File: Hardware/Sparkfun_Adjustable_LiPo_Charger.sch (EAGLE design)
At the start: 25 parts, among them SW1 DIP-06, U1 MCP73831

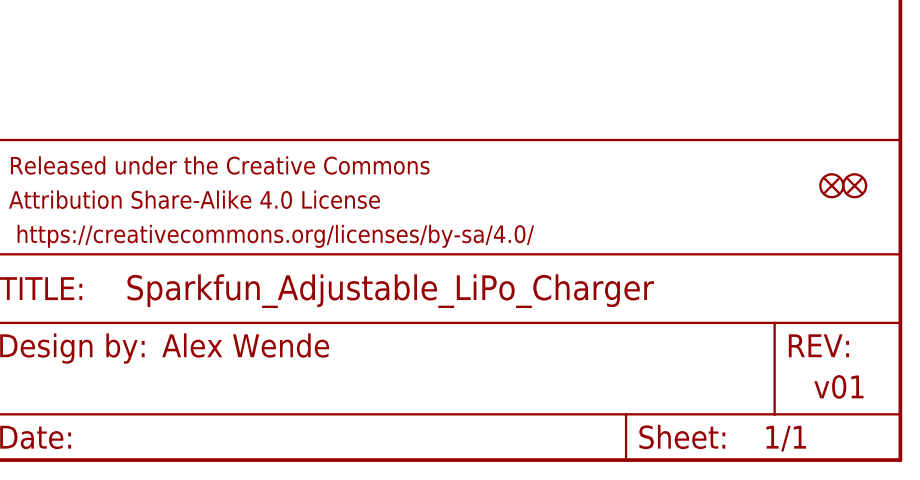
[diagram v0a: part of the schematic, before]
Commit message: Design Review Changes
Replaced PTH coin cell holder with SMD
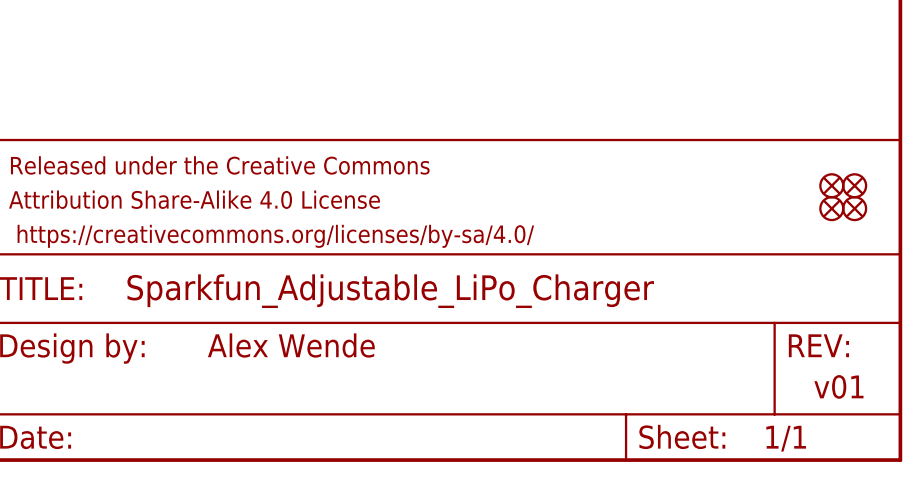
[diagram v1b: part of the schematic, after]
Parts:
- added FD3, FD4: FIDUCIALUFIDUCIAL, SparkFun-Aesthetics:FIDUCIALUFIDUCIAL
- BT1: device SparkFun-Batteries:BATTERY-24.5MM_PTH -> SparkFun-Batteries:BATTERY-24.5MM_SMD
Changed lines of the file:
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@@
 <grid distance="0.1" unitdist="inch" unit="inch" style="lines" multiple="1" display="no" altdistance="0.01" altunitdist="inch" altunit="inch"/>
 <layers>
-<layer number="1" name="Top" color="4" fill="1" visible="yes" active="no"/>
-<layer number="2" name="Route2" color="1" fill="3" visible="yes" active="no"/>
-<layer number="3" name="Route3" color="4" fill="3" visible="yes" active="no"/>
-<layer number="4" name="Route4" color="1" fill="4" visible="yes" active="no"/>
-<layer number="5" name="Route5" color="4" fill="4" visible="yes" active="no"/>
-<layer number="6" name="Route6" color="1" fill="8" visible="yes" active="no"/>
-<layer number="7" name="Route7" color="4" fill="8" visible="yes" active="no"/>
-<layer number="8" name="Route8" color="1" fill="2" visible="yes" active="no"/>
-<layer number="9" name="Route9" color="4" fill="2" visible="yes" active="no"/>
-<layer number="10" name="Route10" color="1" fill="7" visible="yes" active="no"/>
-<layer number="11" name="Route11" color="4" fill="7" visible="yes" active="no"/>
-<layer number="12" name="Route12" color="1" fill="5" visible="yes" active="no"/>
-<layer number="13" name="Route13" color="4" fill="5" visible="yes" active="no"/>
-<layer number="14" name="Route14" color="1" fill="6" visible="yes" active="no"/>
-<layer number="15" name="Route15" color="4" fill="6" visible="yes" active="no"/>
-<layer number="16" name="Bottom" color="1" fill="1" visible="yes" active="no"/>
-<layer number="17" name="Pads" color="2" fill="1" visible="yes" active="no"/>
-<layer number="18" name="Vias" color="2" fill="1" visible="yes" active="no"/>
-<layer number="19" name="Unrouted" color="6" fill="1" visible="yes" active="no"/>
-<layer number="20" name="Dimension" color="15" fill="1" visible="yes" active="no"/>
-<layer number="21" name="tPlace" color="16" fill="1" visible="yes" active="no"/>
-<layer number="22" name="bPlace" color="14" fill="1" visible="yes" active="no"/>
-<layer number="23" name="tOrigins" color="15" fill="1" visible="yes" active="no"/>
-<layer number="24" name="bOrigins" color="15" fill="1" visible="yes" active="no"/>
-<layer number="25" name="tNames" color="7" fill="1" visible="yes" active="no"/>
-<layer number="26" name="bNames" color="7" fill="1" visible="yes" active="no"/>
-<layer number="27" name="tValues" color="7" fill="1" visible="yes" active="no"/>
-<layer number="28" name="bValues" color="7" fill="1" visible="yes" active="no"/>
+<layer number="1" name="Top" color="4" fill="1" visible="no" active="no"/>
+<layer number="2" name="Route2" color="1" fill="3" visible="no" active="no"/>
+<layer number="3" name="Route3" color="4" fill="3" visible="no" active="no"/>
+<layer number="4" name="Route4" color="1" fill="4" visible="no" active="no"/>
+<layer number="5" name="Route5" color="4" fill="4" visible="no" active="no"/>
+<layer number="6" name="Route6" color="1" fill="8" visible="no" active="no"/>
+<layer number="7" name="Route7" color="4" fill="8" visible="no" active="no"/>
+<layer number="8" name="Route8" color="1" fill="2" visible="no" active="no"/>
+<layer number="9" name="Route9" color="4" fill="2" visible="no" active="no"/>
+<layer number="10" name="Route10" color="1" fill="7" visible="no" active="no"/>
+<layer number="11" name="Route11" color="4" fill="7" visible="no" active="no"/>
+<layer number="12" name="Route12" color="1" fill="5" visible="no" active="no"/>
+<layer number="13" name="Route13" color="4" fill="5" visible="no" active="no"/>
+<layer number="14" name="Route14" color="1" fill="6" visible="no" active="no"/>
+<layer number="15" name="Route15" color="4" fill="6" visible="no" active="no"/>
+<layer number="16" name="Bottom" color="1" fill="1" visible="no" active="no"/>
+<layer number="17" name="Pads" color="2" fill="1" visible="no" active="no"/>
+<layer number="18" name="Vias" color="2" fill="1" visible="no" active="no"/>
+<layer number="19" name="Unrouted" color="6" fill="1" visible="no" active="no"/>
+<layer number="20" name="Dimension" color="15" fill="1" visible="no" active="no"/>
+<layer number="21" name="tPlace" color="16" fill="1" visible="no" active="no"/>
+<layer number="22" name="bPlace" color="14" fill="1" visible="no" active="no"/>
+<layer number="23" name="tOrigins" color="15" fill="1" visible="no" active="no"/>
+<layer number="24" name="bOrigins" color="15" fill="1" visible="no" active="no"/>
+<layer number="25" name="tNames" color="7" fill="1" visible="no" active="no"/>
+<layer number="26" name="bNames" color="7" fill="1" visible="no" active="no"/>
+<layer number="27" name="tValues" color="7" fill="1" visible="no" active="no"/>
+<layer number="28" name="bValues" color="7" fill="1" visible="no" active="no"/>
 <layer number="29" name="tStop" color="7" fill="3" visible="no" active="no"/>
 <layer number="30" name="bStop" color="7" fill="6" visible="no" active="no"/>
@@
 <layer number="35" name="tGlue" color="7" fill="4" visible="no" active="no"/>
 <layer number="36" name="bGlue" color="7" fill="5" visible="no" active="no"/>
-<layer number="37" name="tTest" color="7" fill="1" visible="yes" active="no"/>
-<layer number="38" name="bTest" color="7" fill="1" visible="yes" active="no"/>
+<layer number="37" name="tTest" color="7" fill="1" visible="no" active="no"/>
+<layer number="38" name="bTest" color="7" fill="1" visible="no" active="no"/>
 <layer number="39" name="tKeepout" color="4" fill="11" visible="no" active="no"/>
 <layer number="40" name="bKeepout" color="1" fill="11" visible="no" active="no"/>
@@
 <layer number="44" name="Drills" color="7" fill="1" visible="no" active="no"/>
 <layer number="45" name="Holes" color="7" fill="1" visible="no" active="no"/>
-<layer number="46" name="Milling" color="3" fill="1" visible="yes" active="no"/>
-<layer number="47" name="Measures" color="7" fill="1" visible="yes" active="no"/>
-<layer number="48" name="Document" color="7" fill="1" visible="yes" active="no"/>
-<layer number="49" name="Reference" color="7" fill="1" visible="yes" active="no"/>
-<layer number="50" name="dxf" color="7" fill="1" visible="yes" active="no"/>
-<layer number="51" name="tDocu" color="6" fill="1" visible="yes" active="no"/>
-<layer number="52" name="bDocu" color="7" fill="1" visible="yes" active="no"/>
-<layer number="53" name="tGND_GNDA" color="7" fill="9" visible="yes" active="no"/>
-<layer number="54" name="bGND_GNDA" color="1" fill="9" visible="yes" active="no"/>
-<layer number="56" name="wert" color="7" fill="1" visible="yes" active="no"/>
-<layer number="57" name="tCAD" color="7" fill="1" visible="yes" active="no"/>
-<layer number="59" name="tCarbon" color="7" fill="1" visible="yes" active="no"/>
-<layer number="60" name="bCarbon" color="7" fill="1" visible="yes" active="no"/>
+<layer number="46" name="Milling" color="3" fill="1" visible="no" active="no"/>
+<layer number="47" name="Measures" color="7" fill="1" visible="no" active="no"/>
+<layer number="48" name="Document" color="7" fill="1" visible="no" active="no"/>
+<layer number="49" name="Reference" color="7" fill="1" visible="no" active="no"/>
+<layer number="50" name="dxf" color="7" fill="1" visible="no" active="no"/>
+<layer number="51" name="tDocu" color="6" fill="1" visible="no" active="no"/>
+<layer number="52" name="bDocu" color="7" fill="1" visible="no" active="no"/>
+<layer number="53" name="tGND_GNDA" color="7" fill="9" visible="no" active="no"/>
+<layer number="54" name="bGND_GNDA" color="1" fill="9" visible="no" active="no"/>
+<layer number="56" name="wert" color="7" fill="1" visible="no" active="no"/>
+<layer number="57" name="tCAD" color="7" fill="1" visible="no" active="no"/>
+<layer number="59" name="tCarbon" color="7" fill="1" visible="no" active="no"/>
+<layer number="60" name="bCarbon" color="7" fill="1" visible="no" active="no"/>
 <layer number="90" name="Modules" color="5" fill="1" visible="yes" active="yes"/>
 <layer number="91" name="Nets" color="2" fill="1" visible="yes" active="yes"/>
@@
 <part name="J1" library="SparkFun-Connectors" deviceset="JST_2MM_MALE" device=""/>
 <part name="J2" library="SparkFun-Connectors" deviceset="CONN_02" device="1X02_NO_SILK"/>
-<part name="BT1" library="SparkFun-Batteries" deviceset="BATTERY" device="-24.5MM_PTH"/>
+<part name="BT1" library="SparkFun-Batteries" deviceset="BATTERY" device="-24.5MM_SMD"/>
 <part name="GND2" library="SparkFun-PowerSymbols" deviceset="GND" device=""/>
 <part name="GND4" library="SparkFun-PowerSymbols" deviceset="GND" device=""/>
@@
 <part name="GND10" library="SparkFun-PowerSymbols" deviceset="GND" device=""/>
 <part name="SUPPLY8" library="SparkFun-PowerSymbols" deviceset="VCC" device=""/>
+<part name="FD3" library="SparkFun-Aesthetics" deviceset="FIDUCIAL" device="UFIDUCIAL"/>
+<part name="FD4" library="SparkFun-Aesthetics" deviceset="FIDUCIAL" device="UFIDUCIAL"/>
 </parts>
 <sheets>
@@
 <wire x1="147.32" y1="109.22" x2="0" y2="109.22" width="0.2032" layer="97" style="shortdash"/>
 <wire x1="147.32" y1="35.56" x2="0" y2="35.56" width="0.2032" layer="97" style="shortdash"/>
-<text x="166.878" y="11.43" size="2.54" layer="94">Alex Wende</text>
+<text x="171.958" y="11.43" size="2.54" layer="94">Alex Wende</text>
 <text x="239.268" y="6.858" size="2.54" layer="94">v01</text>
 <text x="2.54" y="180.34" size="2.54" layer="97">Connectors</text>
@@
 <instance part="GND10" gate="1" x="210.82" y="60.96"/>
 <instance part="SUPPLY8" gate="G$1" x="182.88" y="73.66"/>
+<instance part="FD3" gate="G$1" x="243.84" y="27.94"/>
+<instance part="FD4" gate="G$1" x="241.3" y="27.94"/>
 </instances>
 <busses>

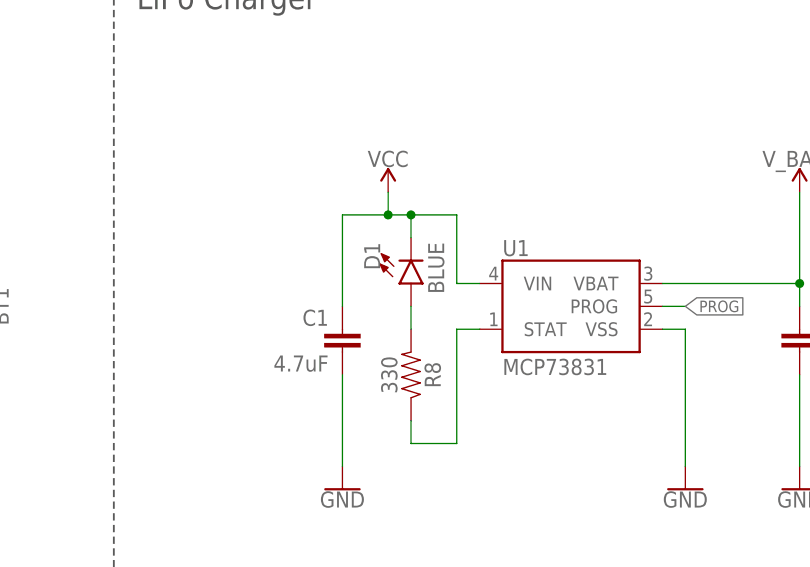
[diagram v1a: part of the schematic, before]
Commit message: Proto Changes
Fixed layout error of D1 to the correct orientation
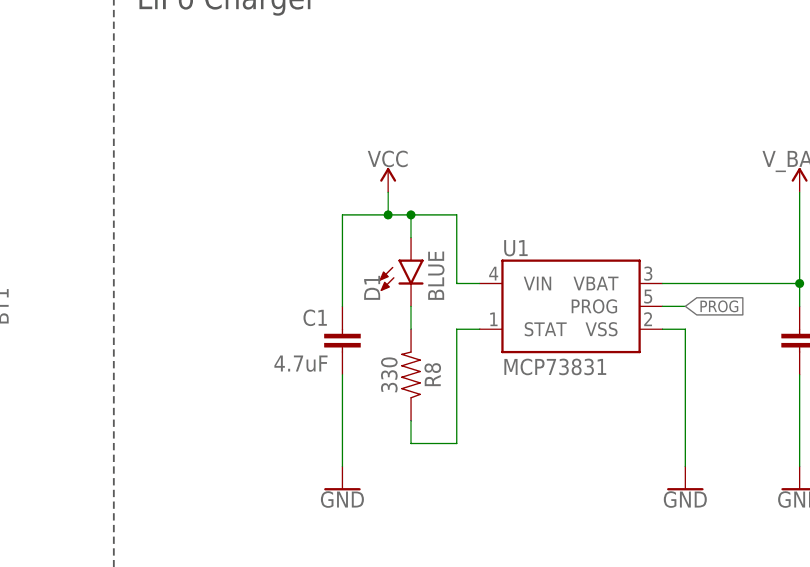
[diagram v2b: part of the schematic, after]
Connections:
- net N$8: now also D1.C; no longer D1.A
- net VCC: now also D1.A; no longer D1.C
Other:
- moved on the sheet: D1
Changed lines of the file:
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@@
 <instance part="C1" gate="G$1" x="172.72" y="142.24" rot="MR0"/>
 <instance part="R8" gate="G$1" x="180.34" y="139.7" rot="MR90"/>
-<instance part="D1" gate="G$1" x="180.34" y="149.86" rot="MR180"/>
+<instance part="D1" gate="G$1" x="180.34" y="152.4"/>
 <instance part="C3" gate="G$1" x="223.52" y="142.24"/>
 <instance part="J1" gate="G$1" x="109.22" y="147.32" rot="MR90"/>
@@
 </segment>
 </net>
-<net name="N$8" class="0">
-<segment>
-<pinref part="R8" gate="G$1" pin="2"/>
-<pinref part="D1" gate="G$1" pin="A"/>
-<wire x1="180.34" y1="144.78" x2="180.34" y2="147.32" width="0.1524" layer="91"/>
-</segment>
-</net>
 <net name="PROG" class="0">
 <segment>
@@
 <wire x1="177.8" y1="157.48" x2="172.72" y2="157.48" width="0.1524" layer="91"/>
 <wire x1="172.72" y1="157.48" x2="172.72" y2="147.32" width="0.1524" layer="91"/>
-<pinref part="D1" gate="G$1" pin="C"/>
-<wire x1="180.34" y1="154.94" x2="180.34" y2="157.48" width="0.1524" layer="91"/>
-<junction x="180.34" y="157.48"/>
 <wire x1="177.8" y1="157.48" x2="177.8" y2="160.02" width="0.1524" layer="91"/>
 <junction x="177.8" y="157.48"/>
 <pinref part="SUPPLY1" gate="G$1" pin="VCC"/>
+<pinref part="D1" gate="G$1" pin="A"/>
+<wire x1="180.34" y1="154.94" x2="180.34" y2="157.48" width="0.1524" layer="91"/>
+<junction x="180.34" y="157.48"/>
 </segment>
 <segment>
@@
 </segment>
 </net>
+<net name="N$8" class="0">
+<segment>
+<pinref part="R8" gate="G$1" pin="2"/>
+<pinref part="D1" gate="G$1" pin="C"/>
+<wire x1="180.34" y1="147.32" x2="180.34" y2="144.78" width="0.1524" layer="91"/>
+</segment>
+</net>
